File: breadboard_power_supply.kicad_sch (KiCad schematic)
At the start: 17 parts, among them J1 Barrel_Jack_Switch, J2 Conn_01x02_Male, J3 Conn_01x02_Male, J4 Screw_Terminal_01x02, J5 Conn_01x03_Male, J6 Conn_01x03_Male, J7 Screw_Terminal_01x02, U1 LM7805_TO220, U2 LM317_TO-220

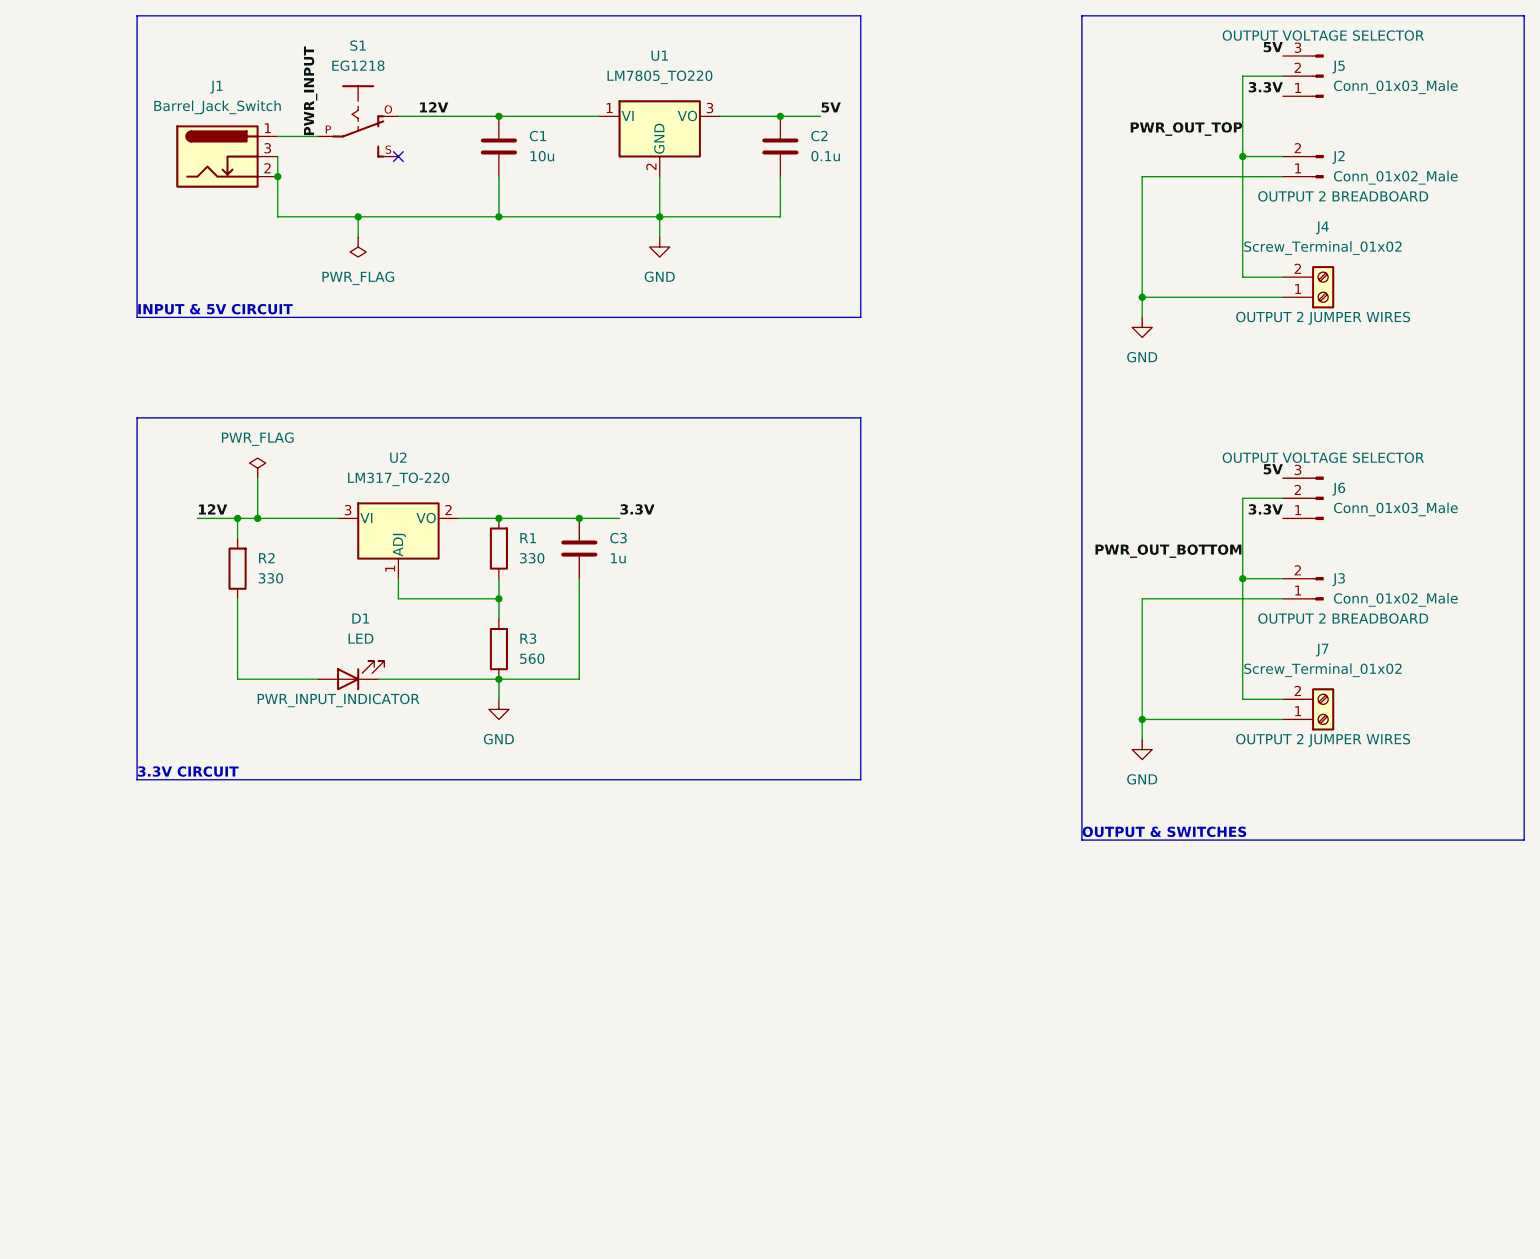
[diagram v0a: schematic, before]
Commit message: back-up recovery
I lost the old document, and tried to bring it back extracting a backups file from Supply_and_Sensors branch
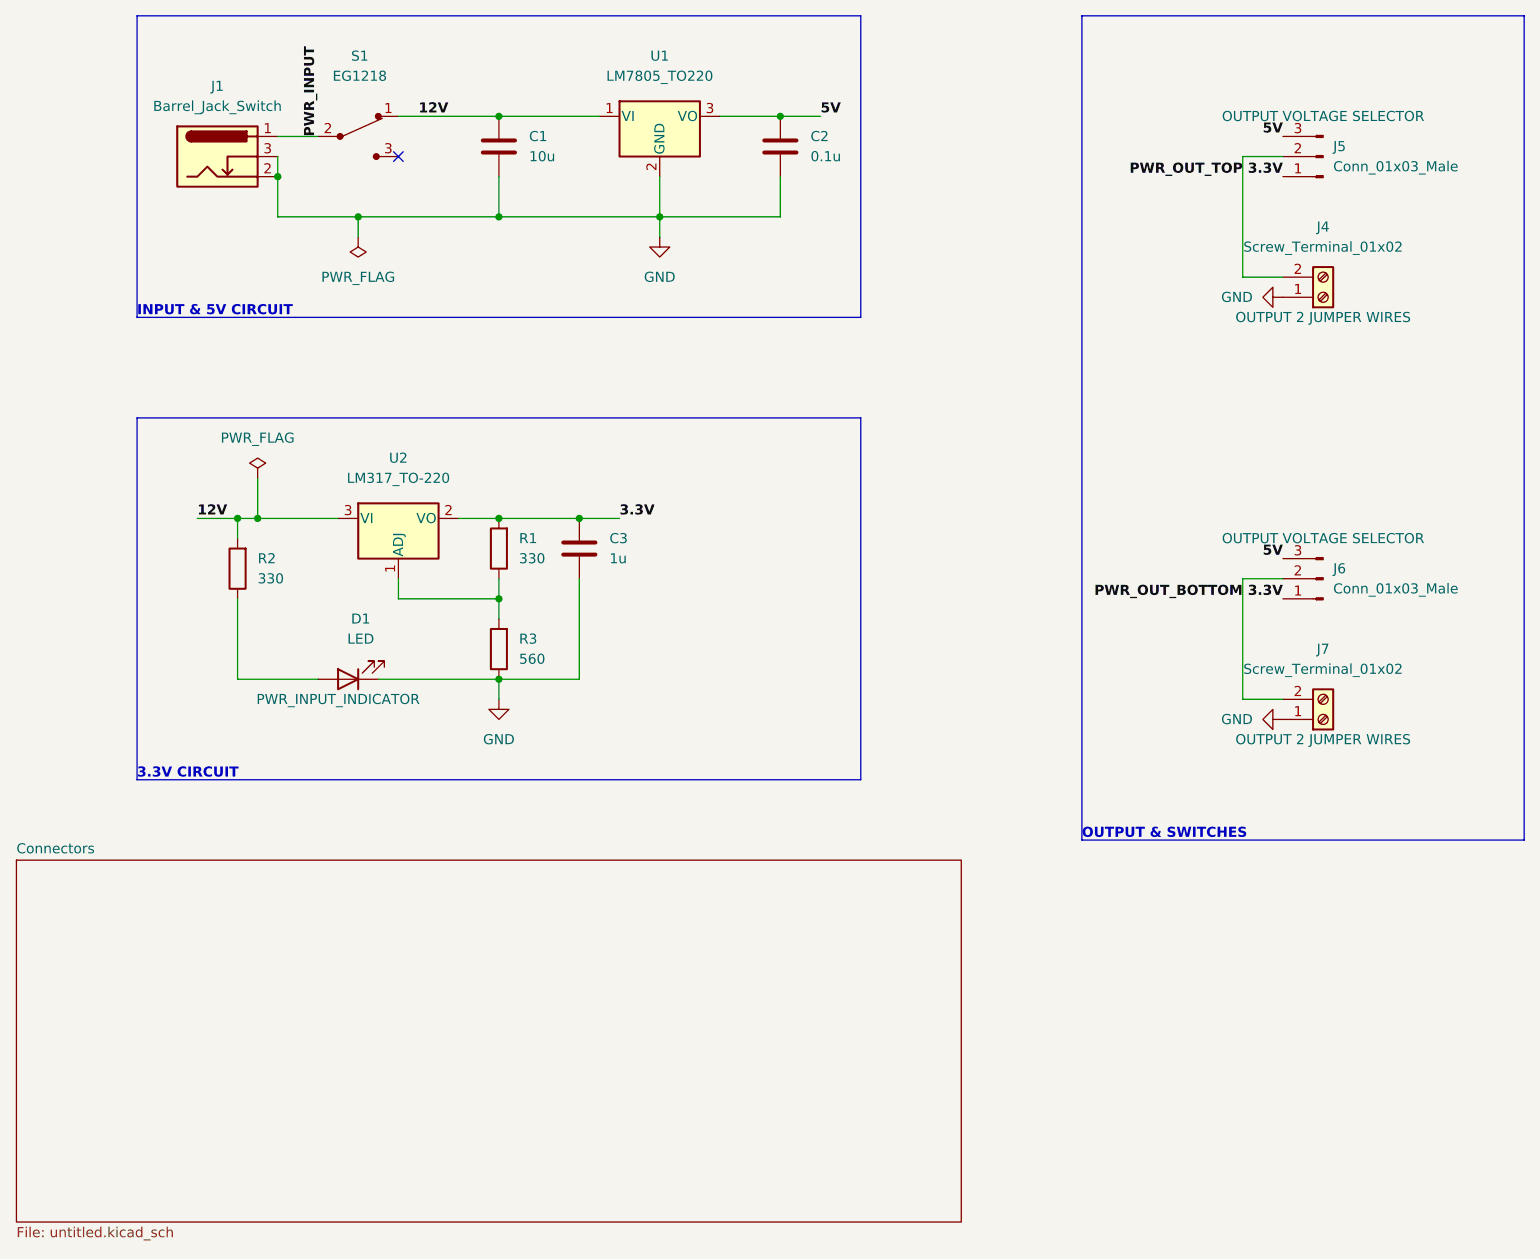
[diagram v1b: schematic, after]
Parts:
- removed J2, J3: Conn_01x02_Male, Connector_PinHeader_2.54mm:PinHeader_1x02_P2.54mm_Vertical, symbol Connector:Conn_01x02_Male
- removed S1: EG1218, EG1218:EG1218, symbol Slide_Switch:EG1218
- added S1: EG1218, digkey_slide_switch:Switch_Slide_11.6x4mm_EG1218, symbol digkey_slide_switch:EG1218
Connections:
- net 12V: now also S1.1
- net PWR_INPUT: now also S1.2
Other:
- added sheet Connectors (untitled.kicad_sch)
- moved on the sheet: J5, J6

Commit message: Revert "Project Target Description"
This reverts commit 992a993e3ba41f038e621602d57108eb9190e08b.
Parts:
- removed S1: EG1218, digkey_slide_switch:Switch_Slide_11.6x4mm_EG1218, symbol digkey_slide_switch:EG1218
- added J2, J3: Conn_01x02_Male, Connector_PinHeader_2.54mm:PinHeader_1x02_P2.54mm_Vertical, symbol Connector:Conn_01x02_Male
- added S1: EG1218, EG1218:EG1218, symbol Slide_Switch:EG1218
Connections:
- net 12V: now also S1.O
- net GND: now also J2.1 (Pin_1), J3.1 (Pin_1)
- net PWR_INPUT: now also S1.P
- net PWR_OUT_BOTTOM: now also J3.2 (Pin_2)
- net PWR_OUT_TOP: now also J2.2 (Pin_2)
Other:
- removed sheet Connectors
- moved on the sheet: J5, J6
